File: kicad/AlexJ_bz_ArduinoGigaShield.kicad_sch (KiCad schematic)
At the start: 54 parts, among them J1 Conn_01x08, J10 JSIDE_5V, J2 Conn_01x10, J3 Conn_01x08, J4 Conn_01x08, J5 Conn_01x26, J6 Conn_01x08, J7 Conn_01x08, J8 Conn_01x26, J9 JSIDE, U1 SN74LVC541, U2 SN74LVC541, U3 SN74LVC541, U4 SN74AHCT541, U5 SN74LVC4245A, U6 TXB0108PW, U7 TXB0108PW, U8 TXB0108PW, U9 TXB0108PW

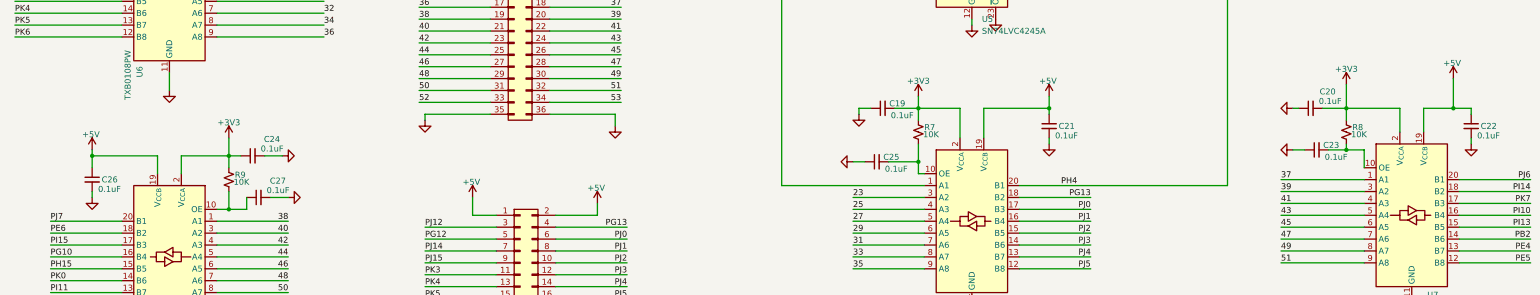
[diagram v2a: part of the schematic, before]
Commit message: Remove C19-C27 extra decoupling caps from schematic
The v0.1 design had 27 caps (3 per TXB0108). With v0.2's single-supply
ICs (U1-U4), only 1 cap per IC is needed. U5 keeps 2 (VCCA+VCCB).
U6-U9 keep 3 each. Total: 18 caps (C1-C18).

Also removes 7 dedicated GND symbols and connecting wires.
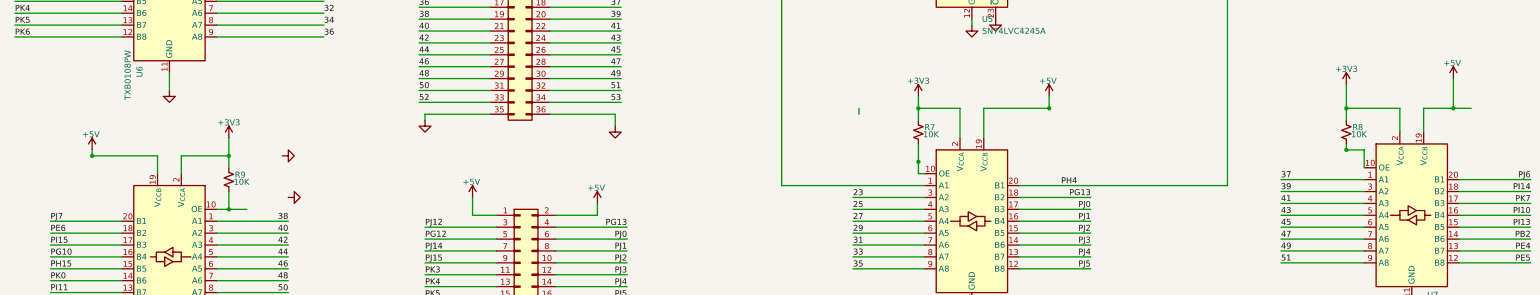
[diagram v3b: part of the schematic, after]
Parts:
- removed C19, C20, C21, C22, C23, C24, C25, C26, C27: 0.1uF, Capacitor_SMD:C_0603_1608Metric, symbol Device:C_Small

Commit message: Add DATA_DIR net, U5 hidden GND pins, and update change log
- Add DATA_DIR label at U5 DIR pin (262.89, 148.59)
- Add DATA_DIR label on Arduino D2 wire (225.0, 93.98) to connect nets
- Add hidden GND pins 7, 17, 22 to SN74LVC4245A lib_symbol
- Update CHANGES-V0.2.md with completed schematic edits and remaining GUI work
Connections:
- net DATA_DIR is gone; now on net 2: U5.2 (DIR)
- net GND: now also U5.17 (GND), U5.22 (GND), U5.7 (GND)
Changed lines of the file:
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@@
+		)
+	)
+	(label "DATA_DIR"
+		(at 225.0 93.98 0)
+		(effects
+			(font
+				(size 1.27 1.27)
+			)
+			(justify left bottom)
 		)
 	)
